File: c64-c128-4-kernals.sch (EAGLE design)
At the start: 16 parts, among them IC1 27C512, IC2 PIC12F629P

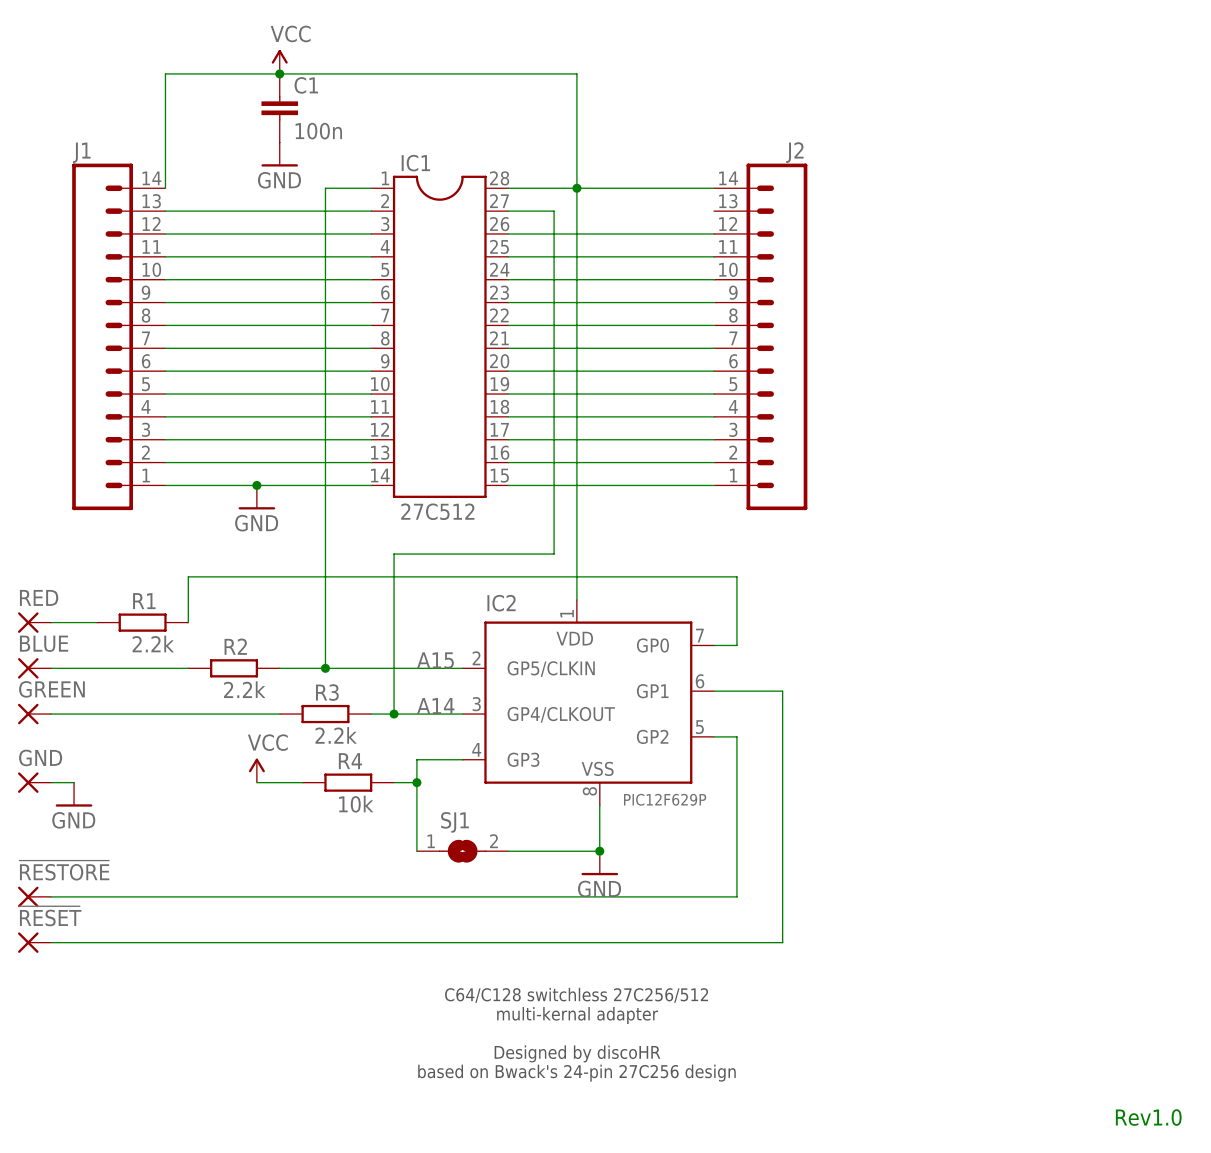
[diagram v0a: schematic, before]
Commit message: removed R4 rearranged signal-pin pairs to allow using weak pull-up for the solder jumper minor design changes improved routing
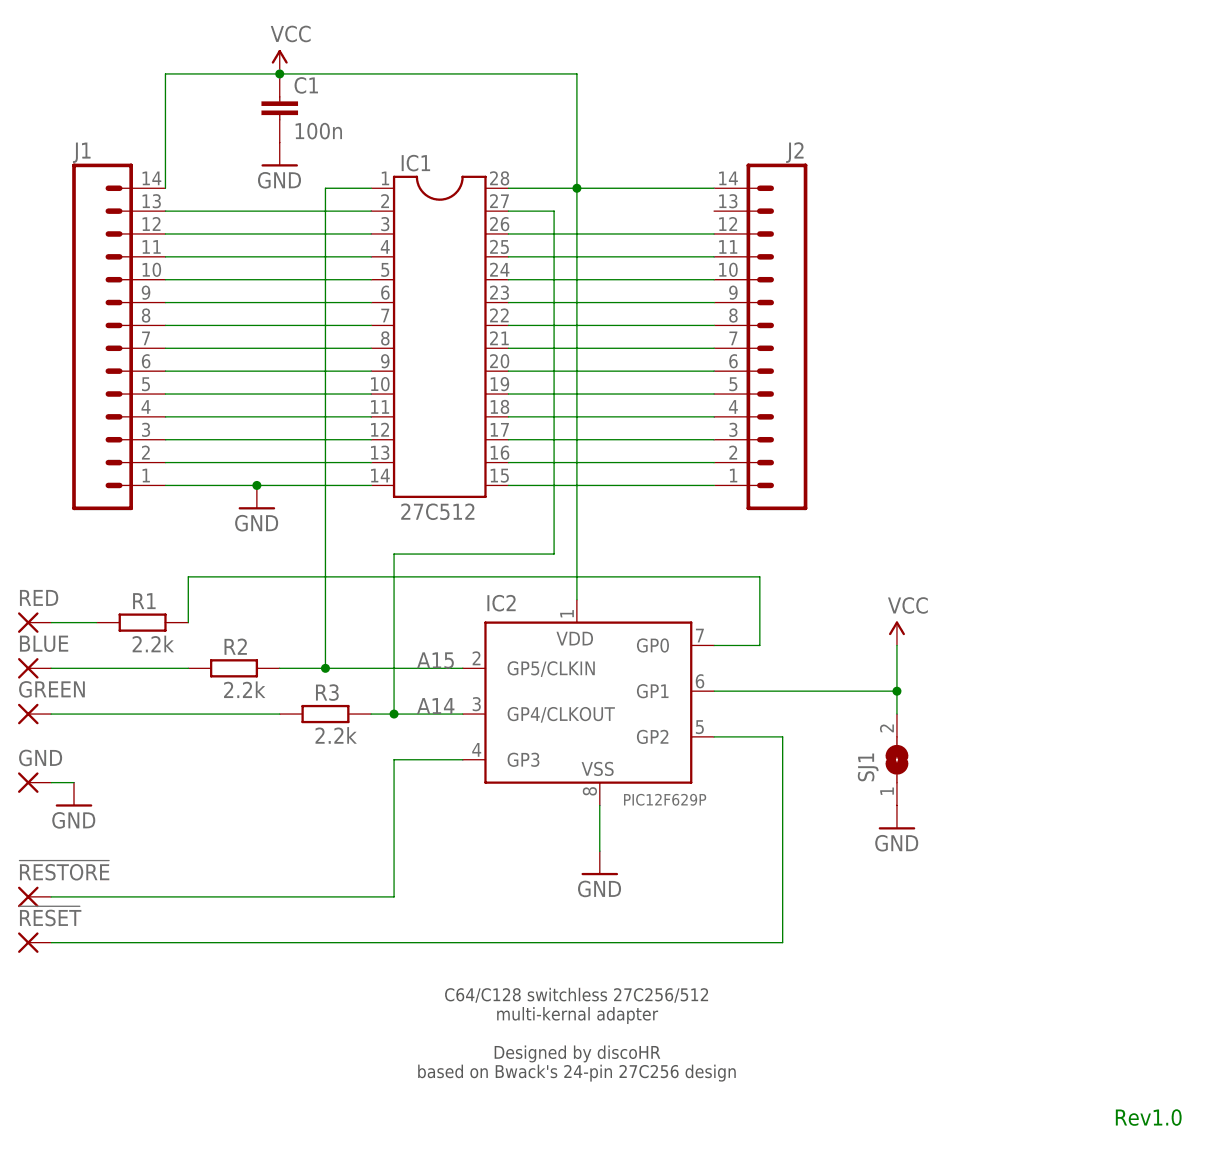
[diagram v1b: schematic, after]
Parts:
- removed R4: 10k, resistor:R-EU_0207/10
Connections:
- removed net N$16: !RESTORE!.P, IC2.GP2
- net GND: now also SJ1.1; no longer SJ1.2
- net N$28: now also IC2.GP2; no longer IC2.GP1
- net N$31: now also !RESTORE!.P; no longer R4.2, SJ1.1
- net VCC: now also IC2.GP1, SJ1.2; no longer R4.1
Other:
- moved on the sheet: SJ1
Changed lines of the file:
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@@
 <part name="SJ1" library="jumper" deviceset="SJ" device=""/>
 <part name="SUPPLY1" library="SparkFun-Aesthetics" deviceset="VCC" device=""/>
-<part name="R4" library="resistor" deviceset="R-EU_" device="0207/10" value="10k"/>
 <part name="GND2" library="SparkFun-Aesthetics" deviceset="GND" device=""/>
+<part name="GND3" library="SparkFun-Aesthetics" deviceset="GND" device=""/>
 </parts>
 <sheets>
@@
 <instance part="GND5" gate="1" x="114.3" y="33.02"/>
 <instance part="FRAME1" gate="G$1" x="0" y="0"/>
-<instance part="SJ1" gate="1" x="99.06" y="35.56"/>
-<instance part="SUPPLY1" gate="G$1" x="76.2" y="43.18"/>
-<instance part="R4" gate="G$1" x="86.36" y="43.18" smashed="yes">
-<attribute name="NAME" x="85.09" y="44.6786" size="1.778" layer="95"/>
-<attribute name="VALUE" x="85.09" y="39.878" size="1.778" layer="96"/>
-</instance>
+<instance part="SJ1" gate="1" x="147.32" y="45.72" rot="R90"/>
+<instance part="SUPPLY1" gate="G$1" x="147.32" y="58.42"/>
 <instance part="GND2" gate="1" x="55.88" y="40.64"/>
+<instance part="GND3" gate="1" x="147.32" y="38.1"/>
 </instances>
 <busses>
@@
 </segment>
 <segment>
+<pinref part="SJ1" gate="1" pin="2"/>
 <pinref part="SUPPLY1" gate="G$1" pin="VCC"/>
-<pinref part="R4" gate="G$1" pin="1"/>
-<wire x1="81.28" y1="43.18" x2="76.2" y2="43.18" width="0.1524" layer="91"/>
+<wire x1="147.32" y1="58.42" x2="147.32" y2="53.34" width="0.1524" layer="91"/>
+<pinref part="IC2" gate="G$1" pin="GP1"/>
+<wire x1="147.32" y1="53.34" x2="147.32" y2="50.8" width="0.1524" layer="91"/>
+<wire x1="127" y1="53.34" x2="147.32" y2="53.34" width="0.1524" layer="91"/>
+<junction x="147.32" y="53.34"/>
 </segment>
 </net>
@@
 <pinref part="GND5" gate="1" pin="GND"/>
 <wire x1="114.3" y1="35.56" x2="114.3" y2="40.64" width="0.1524" layer="91"/>
-<pinref part="SJ1" gate="1" pin="2"/>
-<wire x1="104.14" y1="35.56" x2="114.3" y2="35.56" width="0.1524" layer="91"/>
-<junction x="114.3" y="35.56"/>
 </segment>
 <segment>
@@
 <wire x1="53.34" y1="43.18" x2="55.88" y2="43.18" width="0.1524" layer="91"/>
 <pinref part="GND2" gate="1" pin="GND"/>
+</segment>
+<segment>
+<pinref part="GND3" gate="1" pin="GND"/>
+<pinref part="SJ1" gate="1" pin="1"/>
 </segment>
 </net>
@@
 <segment>
 <pinref part="IC2" gate="G$1" pin="GP0"/>
-<wire x1="129.54" y1="58.42" x2="127" y2="58.42" width="0.1524" layer="91"/>
+<wire x1="132.08" y1="58.42" x2="127" y2="58.42" width="0.1524" layer="91"/>
 <pinref part="R1" gate="G$1" pin="2"/>
 <wire x1="68.58" y1="60.96" x2="68.58" y2="66.04" width="0.1524" layer="91"/>
-<wire x1="68.58" y1="66.04" x2="129.54" y2="66.04" width="0.1524" layer="91"/>
-<wire x1="129.54" y1="66.04" x2="129.54" y2="58.42" width="0.1524" layer="91"/>
-</segment>
-</net>
-<net name="N$16" class="0">
-<segment>
-<pinref part="!RESTORE!" gate="1" pin="P"/>
-<wire x1="53.34" y1="30.48" x2="129.54" y2="30.48" width="0.1524" layer="91"/>
-<wire x1="129.54" y1="30.48" x2="129.54" y2="48.26" width="0.1524" layer="91"/>
-<pinref part="IC2" gate="G$1" pin="GP2"/>
-<wire x1="129.54" y1="48.26" x2="127" y2="48.26" width="0.1524" layer="91"/>
+<wire x1="68.58" y1="66.04" x2="132.08" y2="66.04" width="0.1524" layer="91"/>
+<wire x1="132.08" y1="66.04" x2="132.08" y2="58.42" width="0.1524" layer="91"/>
 </segment>
 </net>
 <net name="N$28" class="0">
 <segment>
-<pinref part="IC2" gate="G$1" pin="GP1"/>
-<wire x1="127" y1="53.34" x2="134.62" y2="53.34" width="0.1524" layer="91"/>
-<wire x1="134.62" y1="53.34" x2="134.62" y2="25.4" width="0.1524" layer="91"/>
 <pinref part="!RESET!" gate="1" pin="P"/>
 <wire x1="134.62" y1="25.4" x2="53.34" y2="25.4" width="0.1524" layer="91"/>
+<pinref part="IC2" gate="G$1" pin="GP2"/>
+<wire x1="127" y1="48.26" x2="134.62" y2="48.26" width="0.1524" layer="91"/>
+<wire x1="134.62" y1="48.26" x2="134.62" y2="25.4" width="0.1524" layer="91"/>
 </segment>
 </net>
@@
 </segment>
 </net>
-<net name="N$31" class="1">
-<segment>
-<pinref part="R4" gate="G$1" pin="2"/>
-<wire x1="93.98" y1="43.18" x2="91.44" y2="43.18" width="0.1524" layer="91"/>
-<wire x1="93.98" y1="43.18" x2="93.98" y2="45.72" width="0.1524" layer="91"/>
+<net name="N$31" class="0">
+<segment>
 <pinref part="IC2" gate="G$1" pin="GP3"/>
-<wire x1="93.98" y1="45.72" x2="99.06" y2="45.72" width="0.1524" layer="91"/>
-<pinref part="SJ1" gate="1" pin="1"/>
-<wire x1="93.98" y1="43.18" x2="93.98" y2="35.56" width="0.1524" layer="91"/>
-<junction x="93.98" y="43.18"/>
-</segment>
-</net>
+<pinref part="!RESTORE!" gate="1" pin="P"/>
+<wire x1="53.34" y1="30.48" x2="91.44" y2="30.48" width="0.1524" layer="91"/>
+<wire x1="91.44" y1="30.48" x2="91.44" y2="45.72" width="0.1524" layer="91"/>
+<wire x1="91.44" y1="45.72" x2="99.06" y2="45.72" width="0.1524" layer="91"/>
+</segment>
+</net>

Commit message: fixed incorrectly connected switch
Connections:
- new net N$16: IC2.GP1, SJ1.2
- net VCC: no longer IC2.GP1, SJ1.2
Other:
- moved on the sheet: SJ1
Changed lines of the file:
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@@
 <part name="FRAME1" library="frames" deviceset="DINA5_L" device=""/>
 <part name="SJ1" library="jumper" deviceset="SJ" device=""/>
-<part name="SUPPLY1" library="SparkFun-Aesthetics" deviceset="VCC" device=""/>
 <part name="GND2" library="SparkFun-Aesthetics" deviceset="GND" device=""/>
 <part name="GND3" library="SparkFun-Aesthetics" deviceset="GND" device=""/>
@@
 <instance part="GND5" gate="1" x="114.3" y="33.02"/>
 <instance part="FRAME1" gate="G$1" x="0" y="0"/>
-<instance part="SJ1" gate="1" x="147.32" y="45.72" rot="R90"/>
-<instance part="SUPPLY1" gate="G$1" x="147.32" y="58.42"/>
+<instance part="SJ1" gate="1" x="139.7" y="53.34" rot="R180"/>
 <instance part="GND2" gate="1" x="55.88" y="40.64"/>
-<instance part="GND3" gate="1" x="147.32" y="38.1"/>
+<instance part="GND3" gate="1" x="147.32" y="45.72"/>
 </instances>
 <busses>
@@
 <pinref part="C1" gate="G$1" pin="1"/>
 </segment>
-<segment>
-<pinref part="SJ1" gate="1" pin="2"/>
-<pinref part="SUPPLY1" gate="G$1" pin="VCC"/>
-<wire x1="147.32" y1="58.42" x2="147.32" y2="53.34" width="0.1524" layer="91"/>
-<pinref part="IC2" gate="G$1" pin="GP1"/>
-<wire x1="147.32" y1="53.34" x2="147.32" y2="50.8" width="0.1524" layer="91"/>
-<wire x1="127" y1="53.34" x2="147.32" y2="53.34" width="0.1524" layer="91"/>
-<junction x="147.32" y="53.34"/>
-</segment>
 </net>
 <net name="GND" class="1">
@@
 </segment>
 <segment>
+<pinref part="SJ1" gate="1" pin="1"/>
 <pinref part="GND3" gate="1" pin="GND"/>
-<pinref part="SJ1" gate="1" pin="1"/>
+<wire x1="144.78" y1="53.34" x2="147.32" y2="53.34" width="0.1524" layer="91"/>
+<wire x1="147.32" y1="53.34" x2="147.32" y2="48.26" width="0.1524" layer="91"/>
 </segment>
 </net>
@@
 </segment>
 </net>
+<net name="N$16" class="0">
+<segment>
+<pinref part="IC2" gate="G$1" pin="GP1"/>
+<pinref part="SJ1" gate="1" pin="2"/>
+<wire x1="127" y1="53.34" x2="134.62" y2="53.34" width="0.1524" layer="91"/>
+</segment>
+</net>

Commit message: added license
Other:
- note added: "C64/C128 switchless 27C256/512 multi-kernal adapter Designed by discoHR based on Bwack's 24-pin 27C256 design CERN Open Hardware License v1.2 http://www.ohwr.org/"
- note removed: "C64/C128 switchless 27C256/512 multi-kernal adapter Designed by discoHR based on Bwack's 24-pin 27C256 design"
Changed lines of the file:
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@@
 <sheet>
 <plain>
-<text x="111.76" y="20.32" size="1.4224" layer="97" align="top-center">C64/C128 switchless 27C256/512
+<text x="111.76" y="22.86" size="1.4224" layer="97" align="top-center">C64/C128 switchless 27C256/512
 multi-kernal adapter
 Designed by discoHR
-based on Bwack's 24-pin 27C256 design</text>
+based on Bwack's 24-pin 27C256 design
+CERN Open Hardware License v1.2
+http://www.ohwr.org/</text>
 <text x="175.26" y="5.08" size="1.778" layer="91" align="bottom-center">Rev1.0</text>
 </plain>

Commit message: moved pin headers to the bottom where they belong
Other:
- note added: "Rev1.1"
- note removed: "Rev1.0"
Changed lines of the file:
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@@
 CERN Open Hardware License v1.2
 http://www.ohwr.org/</text>
-<text x="175.26" y="5.08" size="1.778" layer="91" align="bottom-center">Rev1.0</text>
+<text x="175.26" y="5.08" size="1.778" layer="91" align="bottom-center">Rev1.1</text>
 </plain>
 <instances>

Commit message: using larger pads
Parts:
- IC1: value 27C512 -> 27C256/512; device ic-package:DIL28 -> c64switchless:IC-PACKAGE_EDIT_DIL28ROUND
- IC2: value PIC12F629P -> MICROCHIP_PIC12F629P; device microchip:PIC12F629P -> c64switchless:MICROCHIP_PIC12F629P
- R1, R2, R3: device resistor:R-EU_0207/10 -> c64switchless:RCL_R-EU_0207/10
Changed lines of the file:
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@@
 <part name="J2" library="SparkFun-Connectors" deviceset="M14" device=""/>
 <part name="$1_15_$_2016-09-13_12-02-17" library="SparkFun-Aesthetics" deviceset="VCC" device=""/>
-<part name="IC1" library="ic-package" deviceset="DIL28" device="" value="27C512"/>
-<part name="IC2" library="microchip" deviceset="PIC12F6*" device="P" technology="29"/>
-<part name="R2" library="resistor" deviceset="R-EU_" device="0207/10" value="2.2k"/>
-<part name="R3" library="resistor" deviceset="R-EU_" device="0207/10" value="2.2k"/>
-<part name="R1" library="resistor" deviceset="R-EU_" device="0207/10" value="2.2k"/>
+<part name="IC1" library="c64switchless" deviceset="IC-PACKAGE_EDIT_DIL28" device="ROUND" value="27C256/512"/>
+<part name="IC2" library="c64switchless" deviceset="MICROCHIP_PIC12F6*" device="P" technology="29"/>
+<part name="R2" library="c64switchless" deviceset="RCL_R-EU_" device="0207/10" value="2.2k"/>
+<part name="R3" library="c64switchless" deviceset="RCL_R-EU_" device="0207/10" value="2.2k"/>
+<part name="R1" library="c64switchless" deviceset="RCL_R-EU_" device="0207/10" value="2.2k"/>
 <part name="RED" library="wirepad" deviceset="2,15/1,0" device=""/>
 <part name="BLUE" library="wirepad" deviceset="2,15/1,0" device=""/>

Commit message: bumped resistor values significantly because the LED is still too bright at 6.7k increased the board size a bit and rerouted most of the traces
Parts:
- R1: value 2.2k -> 6.7k
- R2: value 2.2k -> 10k
- R3: value 2.2k -> 12k
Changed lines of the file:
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@@
 <part name="IC1" library="c64switchless" deviceset="IC-PACKAGE_EDIT_DIL28" device="ROUND" value="27C256/512"/>
 <part name="IC2" library="c64switchless" deviceset="MICROCHIP_PIC12F6*" device="P" technology="29"/>
-<part name="R2" library="c64switchless" deviceset="RCL_R-EU_" device="0207/10" value="2.2k"/>
-<part name="R3" library="c64switchless" deviceset="RCL_R-EU_" device="0207/10" value="2.2k"/>
-<part name="R1" library="c64switchless" deviceset="RCL_R-EU_" device="0207/10" value="2.2k"/>
+<part name="R2" library="c64switchless" deviceset="RCL_R-EU_" device="0207/10" value="10k"/>
+<part name="R3" library="c64switchless" deviceset="RCL_R-EU_" device="0207/10" value="12k"/>
+<part name="R1" library="c64switchless" deviceset="RCL_R-EU_" device="0207/10" value="6.7k"/>
 <part name="RED" library="wirepad" deviceset="2,15/1,0" device=""/>
 <part name="BLUE" library="wirepad" deviceset="2,15/1,0" device=""/>

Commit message: using 6.7k value for R1, R2 and R3
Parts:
- R2: value 10k -> 6.7k
- R3: value 12k -> 6.7k
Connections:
- net N$29: now also GREEN.P; no longer BLUE.P
- net N$30: now also BLUE.P; no longer GREEN.P
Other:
- moved on the sheet: BLUE, GREEN
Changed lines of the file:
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@@
 <part name="IC1" library="c64switchless" deviceset="IC-PACKAGE_EDIT_DIL28" device="ROUND" value="27C256/512"/>
 <part name="IC2" library="c64switchless" deviceset="MICROCHIP_PIC12F6*" device="P" technology="29"/>
-<part name="R2" library="c64switchless" deviceset="RCL_R-EU_" device="0207/10" value="10k"/>
-<part name="R3" library="c64switchless" deviceset="RCL_R-EU_" device="0207/10" value="12k"/>
+<part name="R2" library="c64switchless" deviceset="RCL_R-EU_" device="0207/10" value="6.7k"/>
+<part name="R3" library="c64switchless" deviceset="RCL_R-EU_" device="0207/10" value="6.7k"/>
 <part name="R1" library="c64switchless" deviceset="RCL_R-EU_" device="0207/10" value="6.7k"/>
 <part name="RED" library="wirepad" deviceset="2,15/1,0" device=""/>
+<part name="GREEN" library="wirepad" deviceset="2,15/1,0" device=""/>
 <part name="BLUE" library="wirepad" deviceset="2,15/1,0" device=""/>
-<part name="GREEN" library="wirepad" deviceset="2,15/1,0" device=""/>
 <part name="!RESTORE!" library="wirepad" deviceset="2,15/1,0" device=""/>
 <part name="!RESET!" library="wirepad" deviceset="2,15/1,0" device=""/>
@@
 </instance>
 <instance part="RED" gate="1" x="50.8" y="60.96"/>
-<instance part="BLUE" gate="1" x="50.8" y="55.88"/>
-<instance part="GREEN" gate="1" x="50.8" y="50.8"/>
+<instance part="GREEN" gate="1" x="50.8" y="55.88"/>
+<instance part="BLUE" gate="1" x="50.8" y="50.8"/>
 <instance part="!RESTORE!" gate="1" x="50.8" y="30.48"/>
 <instance part="!RESET!" gate="1" x="50.8" y="25.4"/>
@@
 <net name="N$29" class="0">
 <segment>
-<pinref part="BLUE" gate="1" pin="P"/>
+<pinref part="GREEN" gate="1" pin="P"/>
 <pinref part="R2" gate="G$1" pin="1"/>
 <wire x1="53.34" y1="55.88" x2="68.58" y2="55.88" width="0.1524" layer="91"/>
@@
 <segment>
 <pinref part="R3" gate="G$1" pin="1"/>
-<pinref part="GREEN" gate="1" pin="P"/>
+<pinref part="BLUE" gate="1" pin="P"/>
 <wire x1="78.74" y1="50.8" x2="53.34" y2="50.8" width="0.1524" layer="91"/>
 </segment>
